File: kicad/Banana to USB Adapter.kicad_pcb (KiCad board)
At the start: 2 copper layers, 26.1 x 26.6 mm, 22 parts, among them J1 USB_A, J2 Positive, J3 Negative, J4 Data

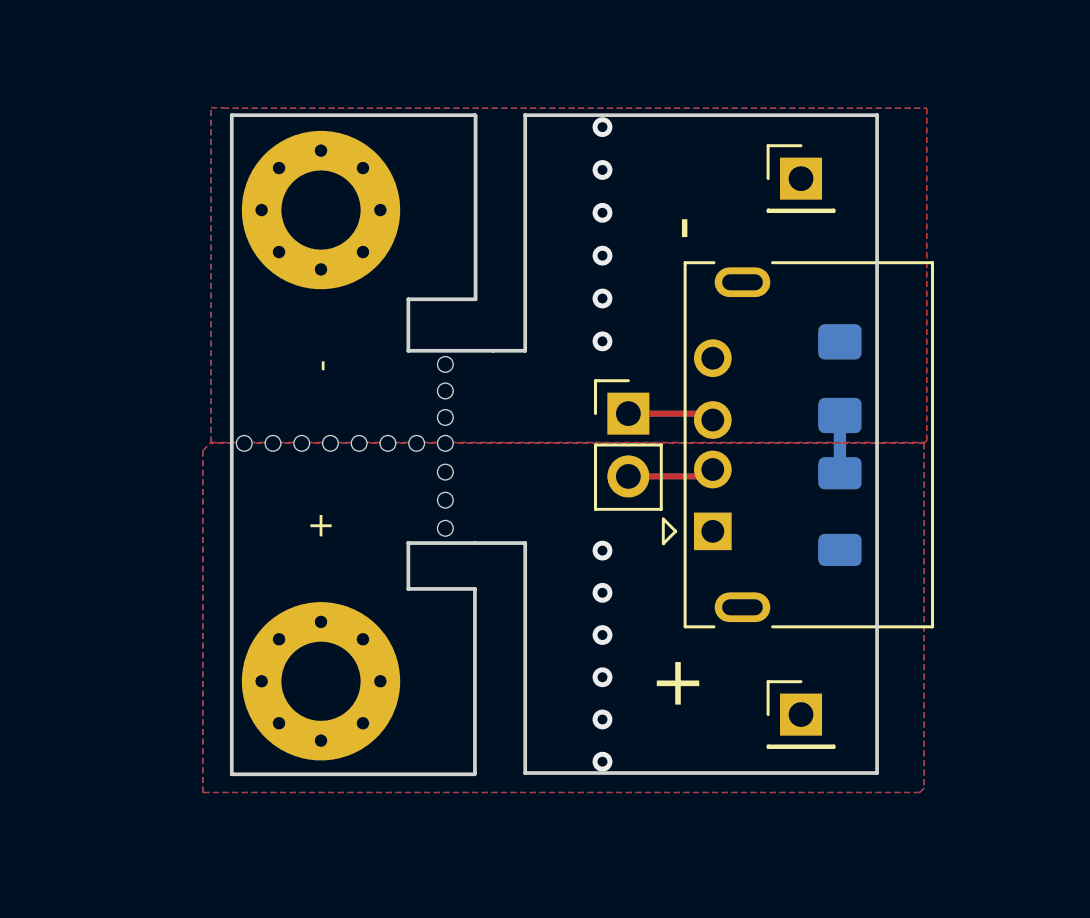
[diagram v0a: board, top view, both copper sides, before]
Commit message: rev2 addresses #2, #3, #5, #6, #7
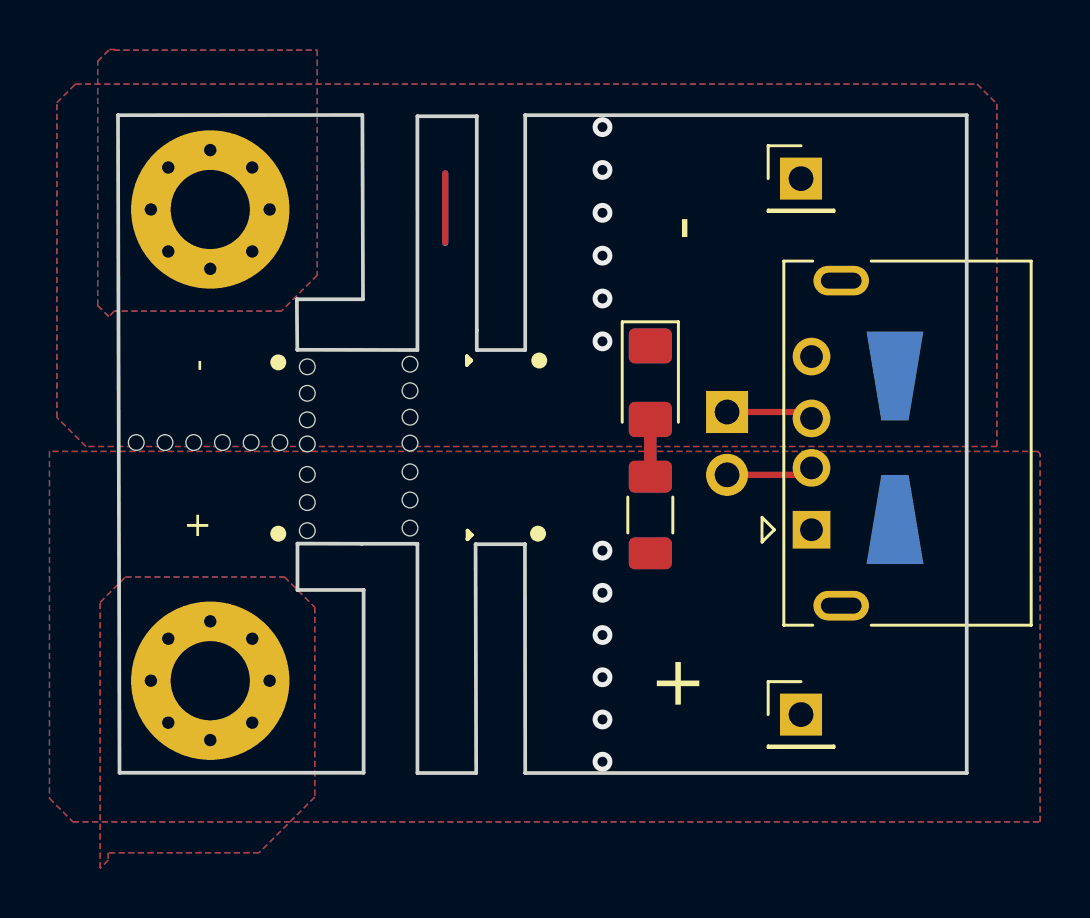
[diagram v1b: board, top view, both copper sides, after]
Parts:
- removed the REF** at (137.5, 99.6)
- added ?: , , F.Cu at (137.1, 96.2)
- added ?: , , F.Cu at (137.1, 102.8)
- added ?: , , F.Cu at (137.1, 98.3)
- added ?: , , F.Cu at (137.1, 97.2)
- added ?: , , F.Cu at (137.1, 99.4)
- added ?: , , F.Cu at (137.1, 101.7)
- added ?: , , F.Cu at (137.1, 100.5)
- added D2: SMBJ6.0A, Diode_SMD:D_SMA-SMB_Universal_Handsoldering, B.Cu at (156.7, 99.5)
- D1, R1: moved to F.Cu
- J4: moved to B.Cu
- moved D1 7.67 mm to (146.8, 96.9)
- moved R1 7.67 mm to (146.8, 102.3)
- moved REF** 5.58 mm to (133.1, 98.6)
- moved REF** 5.58 mm to (133.1, 100.8)
- moved REF** 5.58 mm to (133.1, 102.0)
- moved REF** 5.58 mm to (133.1, 97.6)
- moved REF** 5.58 mm to (133.1, 103.1)
- moved REF** 5.58 mm to (133.1, 96.5)
- moved REF** 5.58 mm to (133.1, 99.6)
- moved H1 4.48 mm to (129.0, 109.0)
- moved H2 4.48 mm to (129.0, 89.9)
- moved REF** 4.37 mm to (126.1, 99.5)
- moved REF** 4.37 mm to (127.3, 99.5)
- moved REF** 4.37 mm to (129.6, 99.5)
- moved REF** 4.37 mm to (131.9, 99.5)
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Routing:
- net GND: track 0.00 -> 5.60 mm
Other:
- board size 26.1 x 26.6 mm -> 34.3 x 26.6 mm
- board text added: "@baldengineer rev2"
- board text removed: "2023-01-20 @baldengineer"
